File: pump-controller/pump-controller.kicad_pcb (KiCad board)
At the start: 2 copper layers, 43.6 x 43.6 mm, 32 parts, among them J1 Conn_02x03_Odd_Even, J2 Conn_01x05_Male, J3 Conn_02x02_Odd_Even, Q1 AO3400A, SW1 SW_Push, U1 ESP32-C3-MINI-1, U3 AP63203WU

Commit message: Trivial tweaks, added version number.
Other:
- board text added: "pdw pump controller v1.2"
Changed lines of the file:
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@@
+		)
+	)
+	(gr_text "pdw pump controller v1.2"
+		(at 223.97 118.865 90)
+		(layer "F.SilkS")
+		(effects
+			(font
+				(size 0.8 0.8)
+				(thickness 0.15)
+				(bold yes)
+			)
+			(justify left bottom)
 		)
 	)
@@
 	)
 	(segment
-		(start 202.607003 109.165102)
-		(end 202.607003 108.139797)
-		(width 0.25)
-		(layer "F.Cu")
-		(net 20)
-	)
-	(segment
 		(start 200.1652 109.5402)
 		(end 200.1652 109.0322)
@@
 	)
 	(segment
+		(start 202.607003 114.226697)
+		(end 202.607003 108.139797)
+		(width 0.25)
+		(layer "F.Cu")
+		(net 20)
+	)
+	(segment
 		(start 198.5966 110.7218)
 		(end 198.9836 110.7218)
@@
 	)
 	(segment
-		(start 202.82 109.378099)
-		(end 202.607003 109.165102)
-		(width 0.25)
-		(layer "F.Cu")
-		(net 20)
-	)
-	(segment
-		(start 202.82 114.0137)
-		(end 202.82 109.378099)
+		(start 201.795 115.0387)
+		(end 202.607003 114.226697)
 		(width 0.25)
 		(layer "F.Cu")
@@
 		(start 198.9836 110.7218)
 		(end 199.8858 109.8196)
-		(width 0.25)
-		(layer "F.Cu")
-		(net 20)
-	)
-	(segment
-		(start 201.795 115.0387)
-		(end 202.82 114.0137)
 		(width 0.25)
 		(layer "F.Cu")
@@
 	)
 	(segment
-		(start 198.9718 114.7218)
-		(end 200.1218 115.8718)
-		(width 0.25)
-		(layer "F.Cu")
-		(net 42)
-	)
-	(segment
-		(start 200.1218 115.8718)
-		(end 200.1966 115.8718)
+		(start 204.093712 111.446288)
+		(end 204.07 111.47)
 		(width 0.25)
 		(layer "F.Cu")
@@
 	)
 	(segment
-		(start 204.093712 111.446288)
-		(end 204.07 111.47)
-		(width 0.25)
-		(layer "F.Cu")
-		(net 42)
-	)
-	(segment
 		(start 204.093712 109.605584)
 		(end 204.093712 111.446288)
@@
 	)
 	(segment
+		(start 200.5548 116.23)
+		(end 202.51 116.23)
+		(width 0.25)
+		(layer "F.Cu")
+		(net 42)
+	)
+	(segment
 		(start 204.05 112.51)
 		(end 204.05 111.49)
@@
 	(segment
 		(start 198.5966 114.7218)
-		(end 198.9718 114.7218)
+		(end 199.0466 114.7218)
 		(width 0.25)
 		(layer "F.Cu")
@@
 	)
 	(segment
-		(start 200.5548 116.23)
-		(end 202.51 116.23)
-		(width 0.25)
-		(layer "F.Cu")
-		(net 42)
-	)
-	(segment
-		(start 200.1966 115.8718)
+		(start 199.0466 114.7218)
 		(end 200.5548 116.23)
 		(width 0.25)
@@
 		(net 0)
 		(net_name "")
-		(layers "F&B.Cu")
+		(layers "F.Cu" "B.Cu")
 		(hatch edge 0.508)
 		(connect_pads

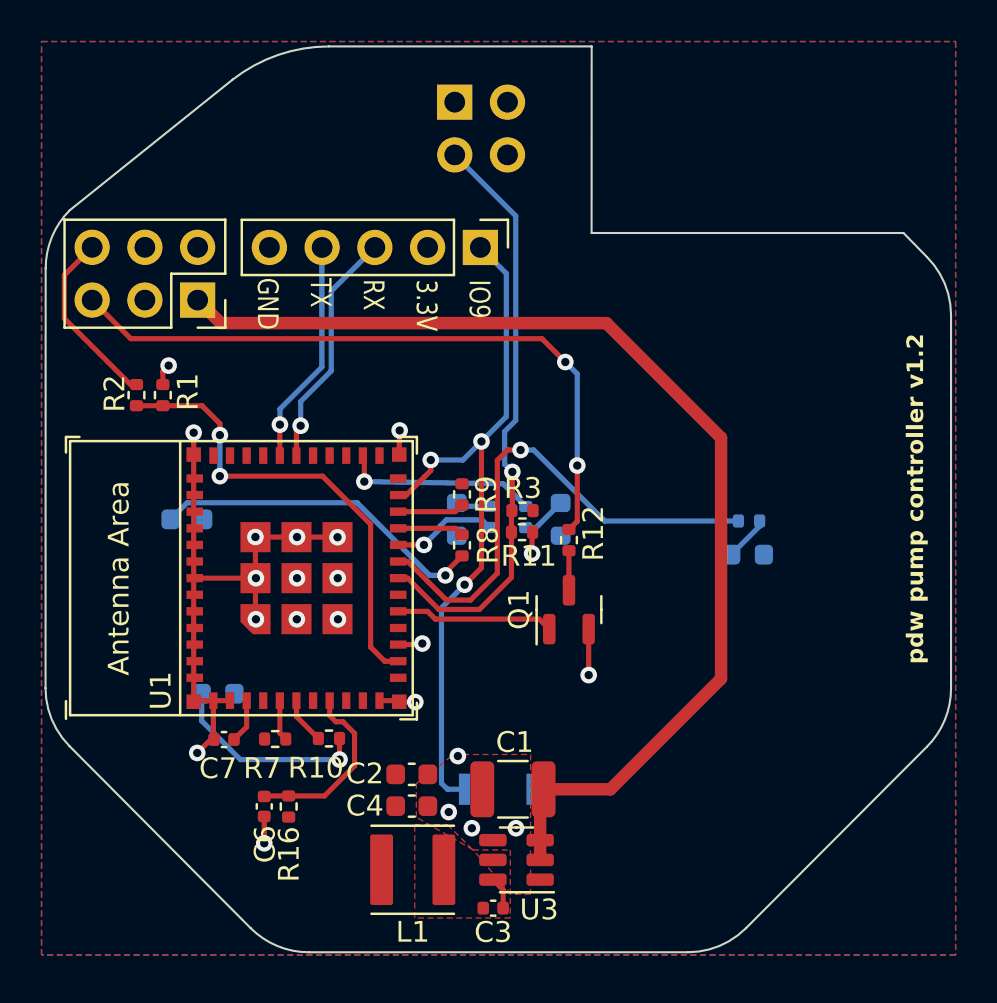
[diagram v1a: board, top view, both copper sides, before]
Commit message: Add missing mounting holes, tweak capacitor footprints.
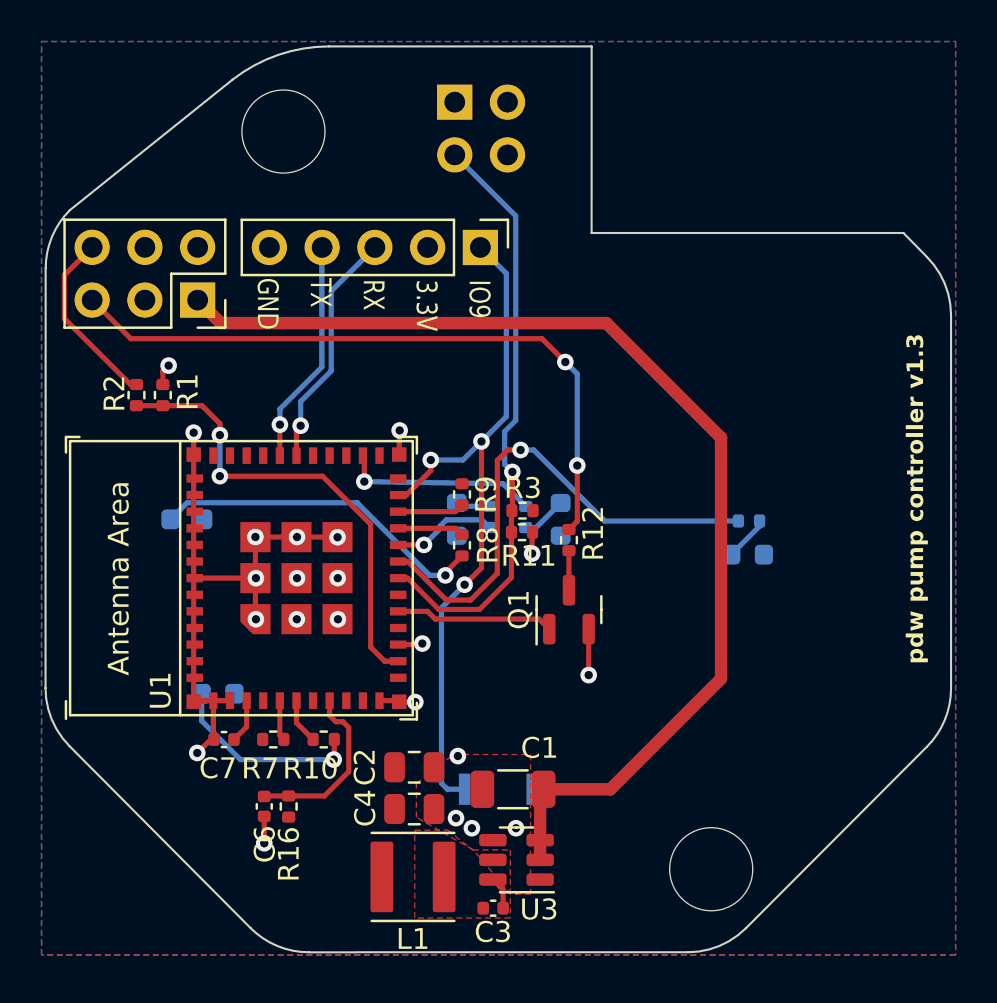
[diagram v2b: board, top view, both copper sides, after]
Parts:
- added H1: MountingHole, MountingHole:MountingHole_4mm, F.Cu at (193.1, 93.2)
- added H2: MountingHole, MountingHole:MountingHole_4mm, F.Cu at (213.7, 128.7)
- C1: footprint Capacitor_SMD:C_1210_3225Metric -> Capacitor_SMD:C_1206_3216Metric
- C2, C4: footprint Capacitor_SMD:C_0603_1608Metric -> Capacitor_SMD:C_0805_2012Metric
- moved C2 0.36 mm to (199.4, 123.8)
- moved L1 0.35 mm to (199.3, 129.1)
- moved R10 0.26 mm to (195.0, 122.5)
- moved C4 0.18 mm to (199.4, 125.8)
- moved R7 0.09 mm to (192.6, 122.5)
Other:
- board text added: "pdw pump controller v1.3"
- board text removed: "pdw pump controller v1.2"

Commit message: Change switch, update zones.
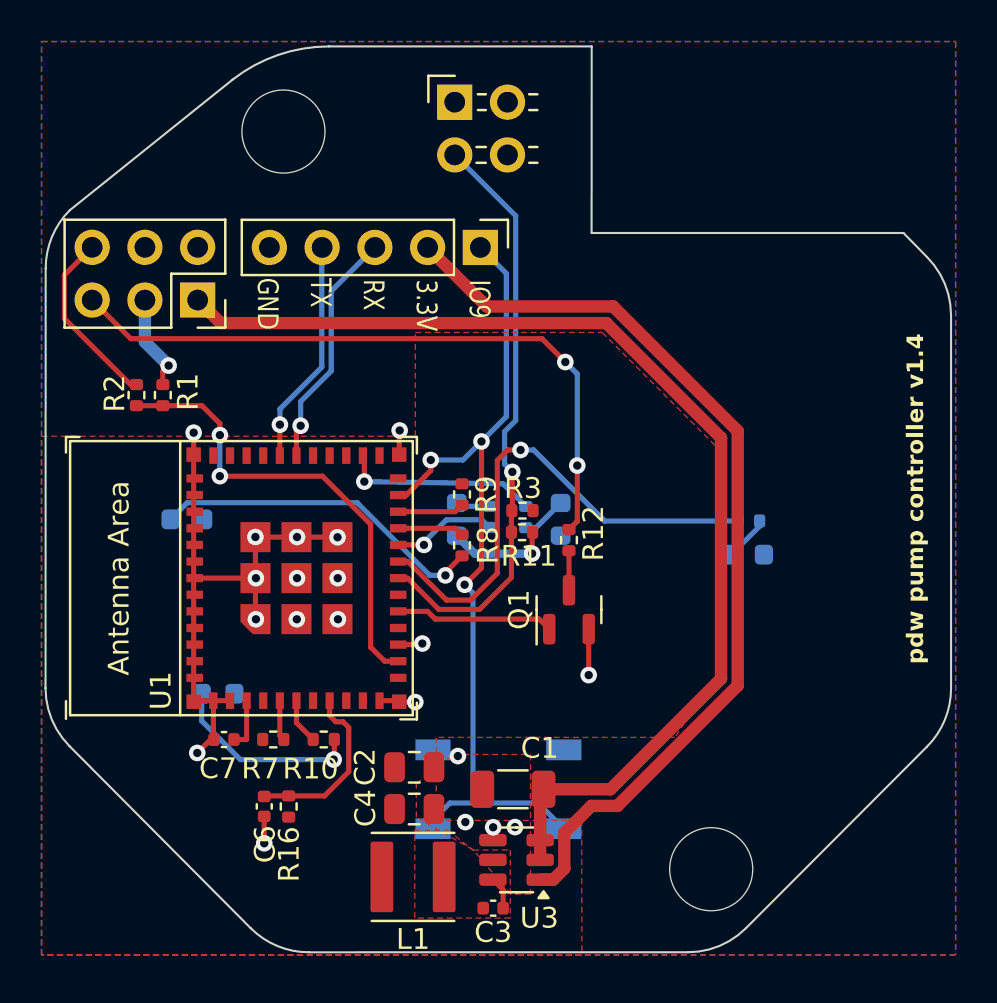
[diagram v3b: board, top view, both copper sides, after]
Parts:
- SW1: footprint utility-meter:TS193206BK701SMTTR67 -> Button_Switch_SMD:SW_SPST_TL3342
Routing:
- net +3.3V: track 2.20 -> 47.8 mm
- net GND: track 38.1 -> 45.7 mm
- net /GPIO9: track 34.2 -> 41.2 mm
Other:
- board text added: "pdw pump controller v1.4"
- board text removed: "pdw pump controller v1.3"

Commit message: Revert to previous switch.
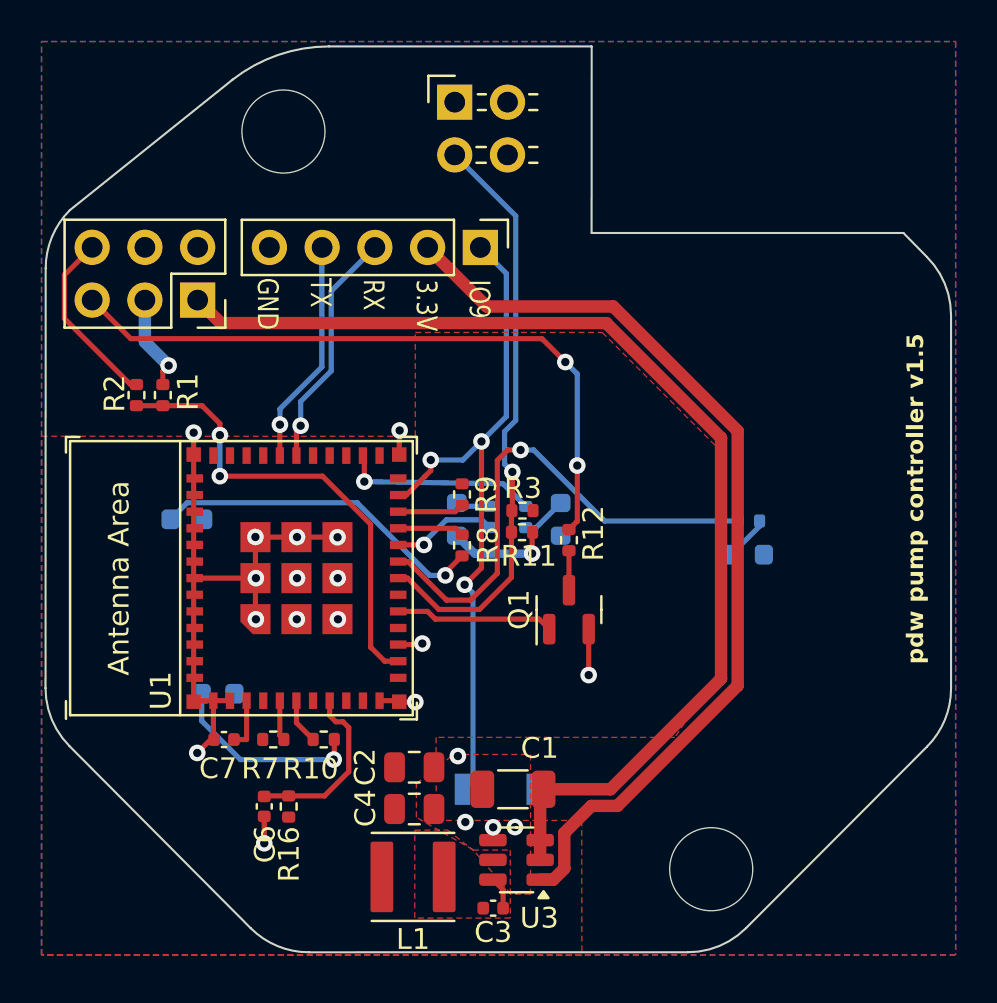
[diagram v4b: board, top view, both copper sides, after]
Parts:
- SW1: footprint Button_Switch_SMD:SW_SPST_TL3342 -> pdw:SW_SPST_3.5x2.0
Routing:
- net /GPIO9: track 41.2 -> 33.3 mm
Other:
- board text added: "pdw pump controller v1.5"
- board text removed: "pdw pump controller v1.4"
